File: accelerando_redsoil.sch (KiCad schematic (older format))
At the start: 8 parts, among them J1 IOA, J2 IOB, J3 USB, J4 SWD, U1 E73-2G4M08S1C-52840

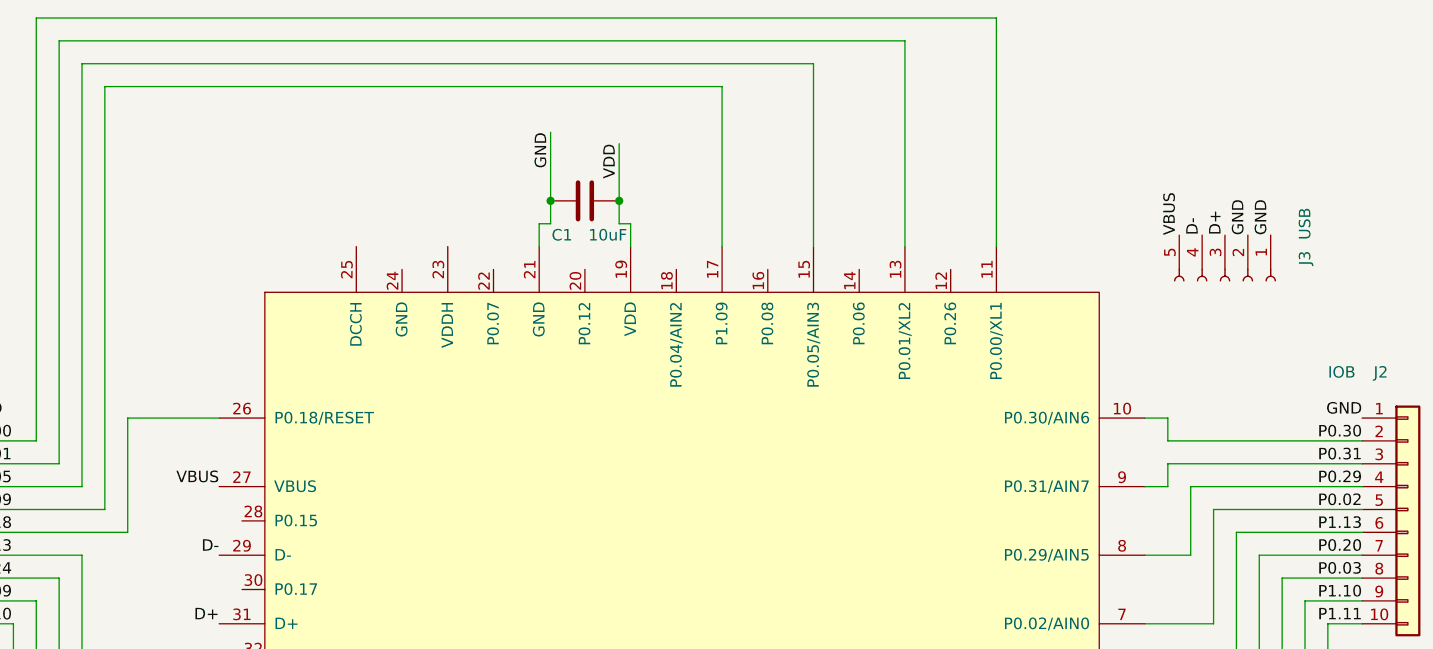
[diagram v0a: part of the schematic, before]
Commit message: Redsoil PCB 1.1 - USB power, Battery conn, JST PH SWD
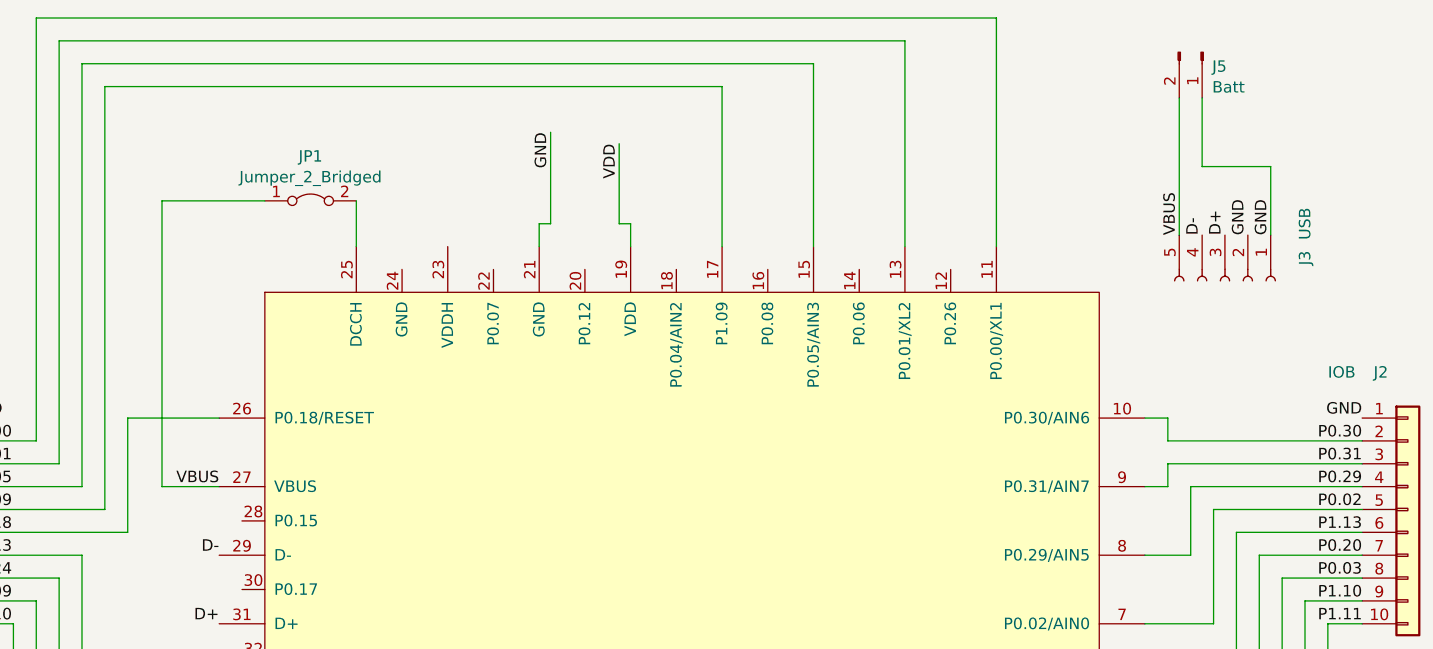
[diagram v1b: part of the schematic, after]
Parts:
- removed C1: 10uF, Capacitor_SMD:C_0805_2012Metric, symbol Device:C
- added J5: Batt, Connector_PinHeader_1.27mm:PinHeader_1x02_P1.27mm_Vertical, symbol Connector:Conn_01x02_Male
- added JP1: Jumper_2_Bridged, Jumper:SolderJumper-2_P1.3mm_Open_RoundedPad1.0x1.5mm, symbol Jumper:Jumper_2_Bridged
- J4: footprint Connector_PinHeader_2.54mm:PinHeader_1x04_P2.54mm_Vertical -> Connector_JST:JST_PH_S4B-PH-K_1x04_P2.00mm_Horizontal
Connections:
- net GND: now also J5.1 (Pin_1)
- net VBUS: now also J5.2 (Pin_2), JP1.1 (A)
- net at U1.25 (DCCH): now also JP1.2 (B)
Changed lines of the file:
@@
 Text Label 3100 2750 0    50   ~ 0
 VDD
-Connection ~ 5950 1800
-Wire Wire Line
-	5950 1900 5950 1800
 Wire Wire Line
 	6000 1900 6000 2000
 Wire Wire Line
 	5950 1900 6000 1900
-Wire Wire Line
-	5950 1550 5950 1800
 Text Label 5950 1550 3    50   ~ 0
 VDD
-Wire Wire Line
-	5650 1800 5650 1900
-Connection ~ 5650 1800
-Wire Wire Line
-	5650 1500 5650 1800
 Text Label 5650 1500 3    50   ~ 0
 GND
@@
 Wire Wire Line
 	5600 2000 5600 1900
-$Comp
-L Device:C C1
-U 1 1 5F26DE07
-P 5800 1800
-F 0 "C1" V 5650 1900 50  0000 C CNN
-F 1 "10uF" V 5650 1700 50  0000 C CNN
-F 2 "Capacitor_SMD:C_0805_2012Metric" H 5838 1650 50  0001 C CNN
-F 3 "~" H 5800 1800 50  0001 C CNN
-	1    5800 1800
-	0    -1   -1   0
-$EndComp
 Text Label 4200 4850 2    50   ~ 0
 SWDCLK
@@
 F 0 "J4" H 2850 5550 50  0000 C CNN
 F 1 "SWD" H 3000 5550 50  0000 C CNN
-F 2 "Connector_PinHeader_2.54mm:PinHeader_1x04_P2.54mm_Vertical" H 2750 5300 50  0001 C CNN
+F 2 "Connector_JST:JST_PH_S4B-PH-K_1x04_P2.00mm_Horizontal" H 2750 5300 50  0001 C CNN
 F 3 "~" H 2750 5300 50  0001 C CNN
 	1    2750 5300
 	0    -1   -1   0
 $EndComp
+$Comp
+L Jumper:Jumper_2_Bridged JP1
+U 1 1 607E5B78
+P 4600 1800
+F 0 "JP1" H 4600 1995 50  0000 C CNN
+F 1 "Jumper_2_Bridged" H 4600 1904 50  0000 C CNN
+F 2 "Jumper:SolderJumper-2_P1.3mm_Open_RoundedPad1.0x1.5mm" H 4600 1800 50  0001 C CNN
+F 3 "~" H 4600 1800 50  0001 C CNN
+	1    4600 1800
+	1    0    0    -1
+$EndComp
+Wire Wire Line
+	4200 3050 3950 3050
+Wire Wire Line
+	3950 3050 3950 1800
+Wire Wire Line
+	3950 1800 4400 1800
+Wire Wire Line
+	4800 1800 4800 2000
+$Comp
+L Connector:Conn_01x02_Male J5
+U 1 1 607EA203
+P 8500 1150
+F 0 "J5" V 8562 1194 50  0000 L CNN
+F 1 "Batt" V 8653 1194 50  0000 L CNN
+F 2 "Connector_PinHeader_1.27mm:PinHeader_1x02_P1.27mm_Vertical" H 8500 1150 50  0001 C CNN
+F 3 "~" H 8500 1150 50  0001 C CNN
+	1    8500 1150
+	0    1    1    0
+$EndComp
+Wire Wire Line
+	8500 1350 8500 1650
+Wire Wire Line
+	8500 1650 8800 1650
+Wire Wire Line
+	8800 1650 8800 1950
+Wire Wire Line
+	8400 1950 8400 1350
+Wire Wire Line
+	5650 1500 5650 1900
+Wire Wire Line
+	5950 1550 5950 1900
 $EndSCHEMATC
